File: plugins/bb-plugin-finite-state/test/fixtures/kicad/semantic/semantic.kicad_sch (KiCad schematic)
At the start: 3 parts, among them U3 TEST_OPAMP

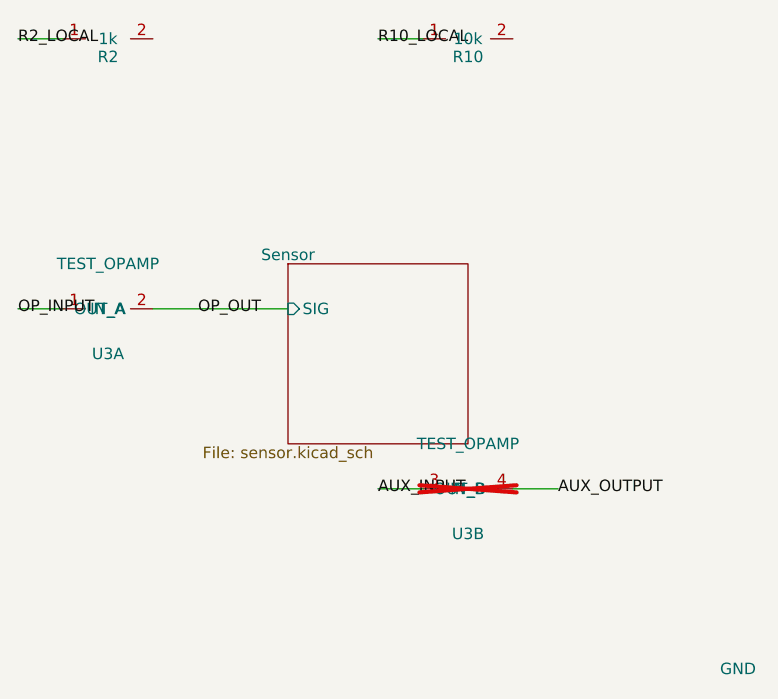
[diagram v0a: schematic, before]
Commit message: Unify repeated local KiCad net labels
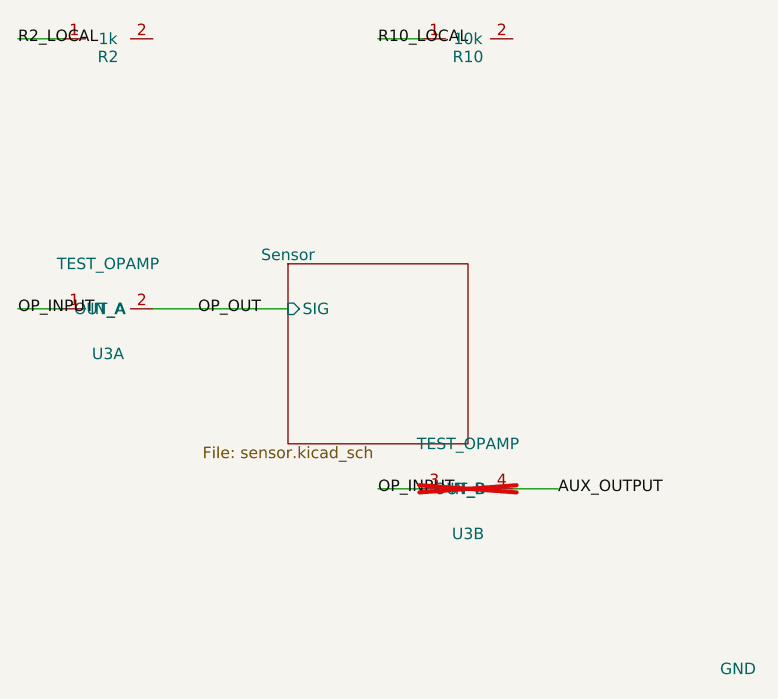
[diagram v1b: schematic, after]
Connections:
- net AUX_INPUT is gone; now on net OP_INPUT: U3.3 (IN_B)
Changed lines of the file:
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@@
   (label "OP_OUT" (at 30 50 0) (effects (font (size 1.27 1.27))))
   (wire (pts (xy 55 70) (xy 50 70)) (stroke (width 0) (type solid)))
-  (label "AUX_INPUT" (at 50 70 0) (effects (font (size 1.27 1.27))))
+  (label "OP_INPUT" (at 50 70 0) (effects (font (size 1.27 1.27))))
   (wire (pts (xy 65 70) (xy 70 70)) (stroke (width 0) (type solid)))
   (label "AUX_OUTPUT" (at 70 70 0) (effects (font (size 1.27 1.27))))
